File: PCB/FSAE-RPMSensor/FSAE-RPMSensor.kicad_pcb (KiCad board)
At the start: 2 copper layers, 4 parts, among them J1 Conn_01x02_Pin, J2 Conn_01x02_Pin

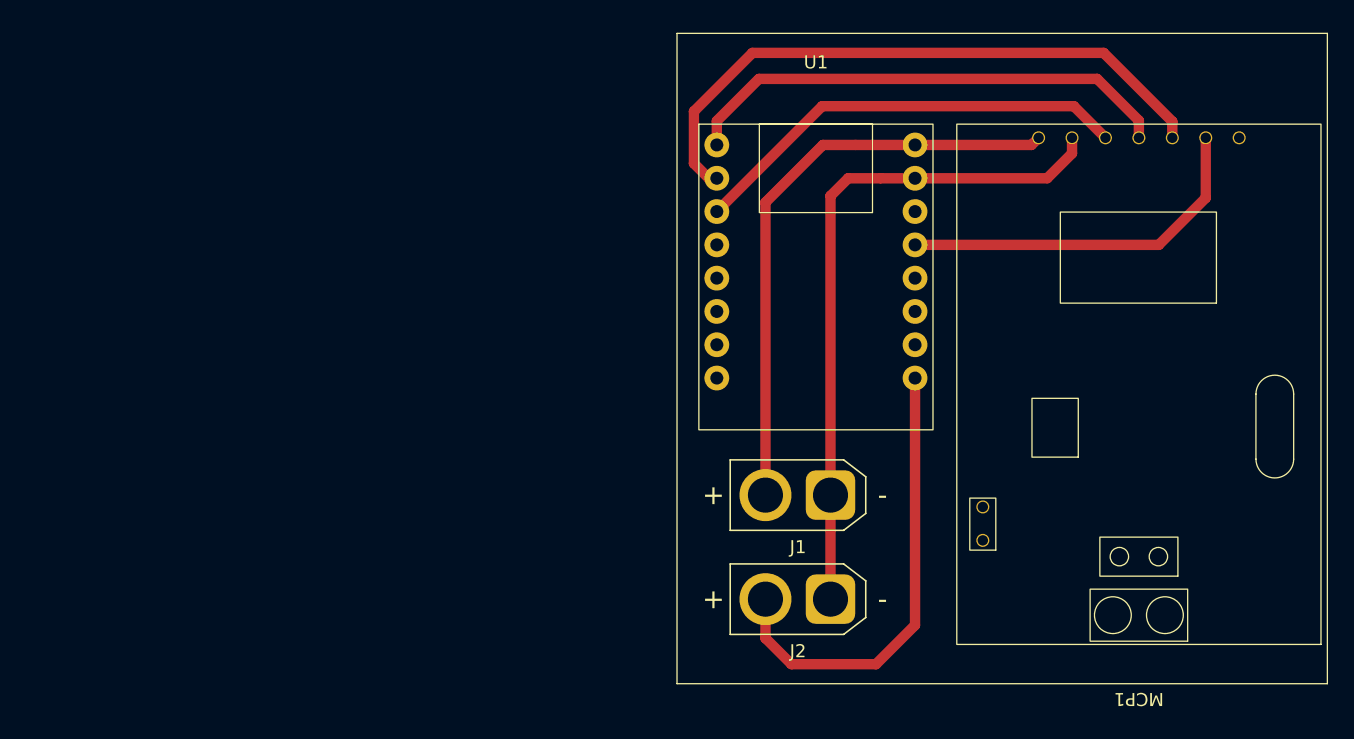
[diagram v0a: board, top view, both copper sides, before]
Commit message: Modificacion de la placa pcb del modelo de comunicacion CAN por uno aisaldo y con fuente buck para el ESP32 C3
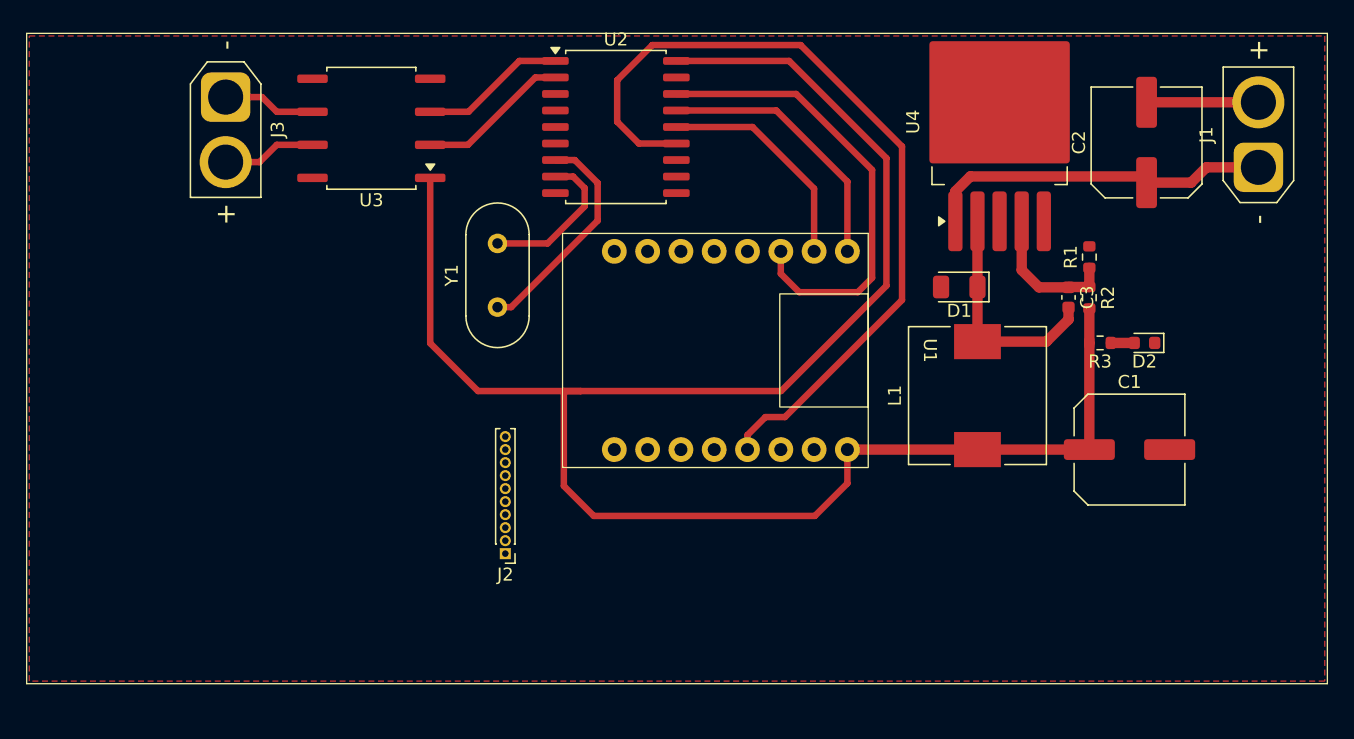
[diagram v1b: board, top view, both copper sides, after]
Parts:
- removed MCP1: MCP2515_Comu_Module, FSAE_Library:MCP2515_Comun_Module
- added C1: 220uF, Capacitor_SMD:C_Elec_8x5.4, F.Cu at (187.0, 90.0)
- added C2: 100uF, Capacitor_SMD:C_Elec_8x5.4, F.Cu at (188.3, 66.4)
- added C3: 15nF, Capacitor_SMD:C_0603_1608Metric, F.Cu at (182.3, 78.3)
- added D1: 1N5822, Diode_SMD:D_1206_3216Metric, F.Cu at (173.9, 77.5)
- added D2: LED, Diode_SMD:D_0603_1608Metric, F.Cu at (188.1, 81.8)
- added J3: Conn_01x02_Pin, Connector_AMASS:AMASS_XT30U-F_1x02_P5.0mm_Vertical, F.Cu at (117.5, 62.9)
- added L1: 470uH, Inductor_SMD:L_10.4x10.4_H4.8, F.Cu at (175.3, 85.8)
- added R1: 1K, Resistor_SMD:R_0603_1608Metric, F.Cu at (183.9, 75.2)
- added R2: 3K1, Resistor_SMD:R_0603_1608Metric, F.Cu at (183.9, 78.3)
- added R3: 1K, Resistor_SMD:R_0603_1608Metric, F.Cu at (184.7, 81.8)
- added U2: MCP2515-xSO, Package_SO:SOIC-18W_7.5x11.6mm_P1.27mm, F.Cu at (147.5, 65.2)
- added U3: ISO1050DUB, Package_SO:SOP-8_6.62x9.15mm_P2.54mm, F.Cu at (128.7, 65.3)
- added U4: LM2596S-ADJ, Package_TO_SOT_SMD:TO-263-5_TabPin3, F.Cu at (177.0, 64.8)
- added Y1: Crystal, Crystal:Crystal_HC18-U_Vertical, F.Cu at (138.4, 79.0)
- J2: value Conn_01x02_Pin -> Conn_01x10_Pin; footprint Connector_AMASS:AMASS_XT30U-F_1x02_P5.0mm_Vertical -> Connector_PinHeader_1.00mm:PinHeader_1x10_P1.00mm_Vertical
- moved J1 41.4 mm to (196.9, 68.3), turned to 90 degrees
- moved J2 25.2 mm to (139.0, 98.0)
- moved U1 9.57 mm to (155.2, 82.4), turned to -90 degrees
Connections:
- J1 pad 2: Net-(J1-Pin_2) -> GND
- J2 pad 1: Net-(J1-Pin_1) -> GPIO21
- J2 pad 2: Net-(J2-Pin_2) -> GPIO20
- U1 pad 1: Net-(MCP1-MISO) -> MISO
- U1 pad 10: Net-(J1-Pin_1) -> GND
- U1 pad 12: Net-(MCP1-SCK) -> SCK
- U1 pad 13: unconnected-(U1-GPIO3/A3-Pad13) -> GPIO3
- U1 pad 14: unconnected-(U1-GPIO2/A2-Pad14) -> GPIO2
- U1 pad 15: unconnected-(U1-GPIO1/A1-Pad15) -> GPIO1
- U1 pad 16: Net-(J2-Pin_2) -> GPIO0
- U1 pad 2: Net-(MCP1-MOSI) -> MOSI
- U1 pad 3: Net-(MCP1-CS) -> CS
- U1 pad 4: unconnected-(U1-GPIO8/SDA-Pad4) -> GPIO8
- U1 pad 5: unconnected-(U1-GPIO9/SCL-Pad5) -> GPIO9
- U1 pad 6: unconnected-(U1-GPIO10-Pad6) -> GPIO10
- U1 pad 7: unconnected-(U1-GPIO20/RX-Pad7) -> GPIO20
- U1 pad 8: unconnected-(U1-GPIO21/TX-Pad8) -> GPIO21
- U1 pad 9: Net-(J1-Pin_2) -> +5V
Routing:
- net +5V: track 0.00 -> 146.2 mm
- net SCK: track 0.00 -> 63.8 mm
- net Net-(MCP1-MOSI): track 48.3 -> 0.00 mm
- net Net-(J1-Pin_2): track 45.6 -> 0.00 mm
- net Net-(MCP1-MISO): track 38.3 -> 0.00 mm
- net Net-(J2-Pin_2): track 35.6 -> 0.00 mm
- net CS: track 0.00 -> 35.6 mm
- net Net-(MCP1-CS): track 34.2 -> 0.00 mm
- net Net-(MCP1-SCK): track 28.5 -> 0.00 mm
- net Net-(J1-Pin_1): track 52.1 -> 26.8 mm
- net MISO: track 0.00 -> 20.8 mm
- net Net-(D1-K): track 0.00 -> 17.9 mm
- net MOSI: track 0.00 -> 17.4 mm
- net Net-(U2-OSC2): track 0.00 -> 17.3 mm
- net GND: track 0.00 -> 13.4 mm
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- added copper zone on F.Cu, net GND
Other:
- board text added: "Revisar tema alimentacion de este modulo dado que al estar aislado requiere doble alimentacion"
